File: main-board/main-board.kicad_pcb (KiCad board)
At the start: 2 copper layers, 210 x 130 mm, 173 parts, among them J1 PWR_SELECT, J10 Conn_02x05_Odd_Even, J11 Conn_02x05_Odd_Even, J12 Conn_02x05_Odd_Even, J13 Conn_02x05_Odd_Even, J14 Conn_02x05_Odd_Even, J15 Conn_02x05_Odd_Even, J16 COMM_3, J17 Modular board connector, J18 PWR_EXT_1, J19 PWR_EXT_2, J2 COMM1, J20 COMM_4, J21 COMM_OUT, J3 ICSP, J4 PULLUP_SEL, J5 COMM_2, J6 PULLDN_SEL, J7 Conn_02x05_Odd_Even, J8 Conn_02x05_Odd_Even, J9 Conn_02x05_Odd_Even, SW1 RESET, SW10 SW_Push, SW11 SW_Push, SW12 SW_SP3T_x08, SW13 SW_Push, SW14 SW_Push, SW15 SW_Push, SW16 SW_Push, SW17 SW_Push, SW18 SW_Push, SW19 SW_Push, SW2 BTN_LEVEL, SW20 SW_Push, SW21 SW_SP3T_x08, SW22 SW_Push, SW23 SW_Push, SW24 SW_Push, SW25 SW_Push, SW26 SW_Push, SW27 SW_Push, SW28 SW_Push, SW29 SW_Push, SW3 LED_GND, SW30 SW_SP3T_x08, SW31 SW_Push, SW32 SW_Push, SW33 SW_Push, SW34 SW_Push, SW35 SW_Push, SW36 SW_Push, SW37 SW_Push, SW38 SW_Push, SW39 SW_SP3T_x08, SW4 SW_Push, SW41 PWR_EN, SW5 SW_Push, SW6 SW_Push, SW7 SW_Push, SW8 SW_Push, SW9 SW_Push, U1 LM2576HVS-5, U2 AP1117-33, U3 AP1117-18, U4 FT232RL

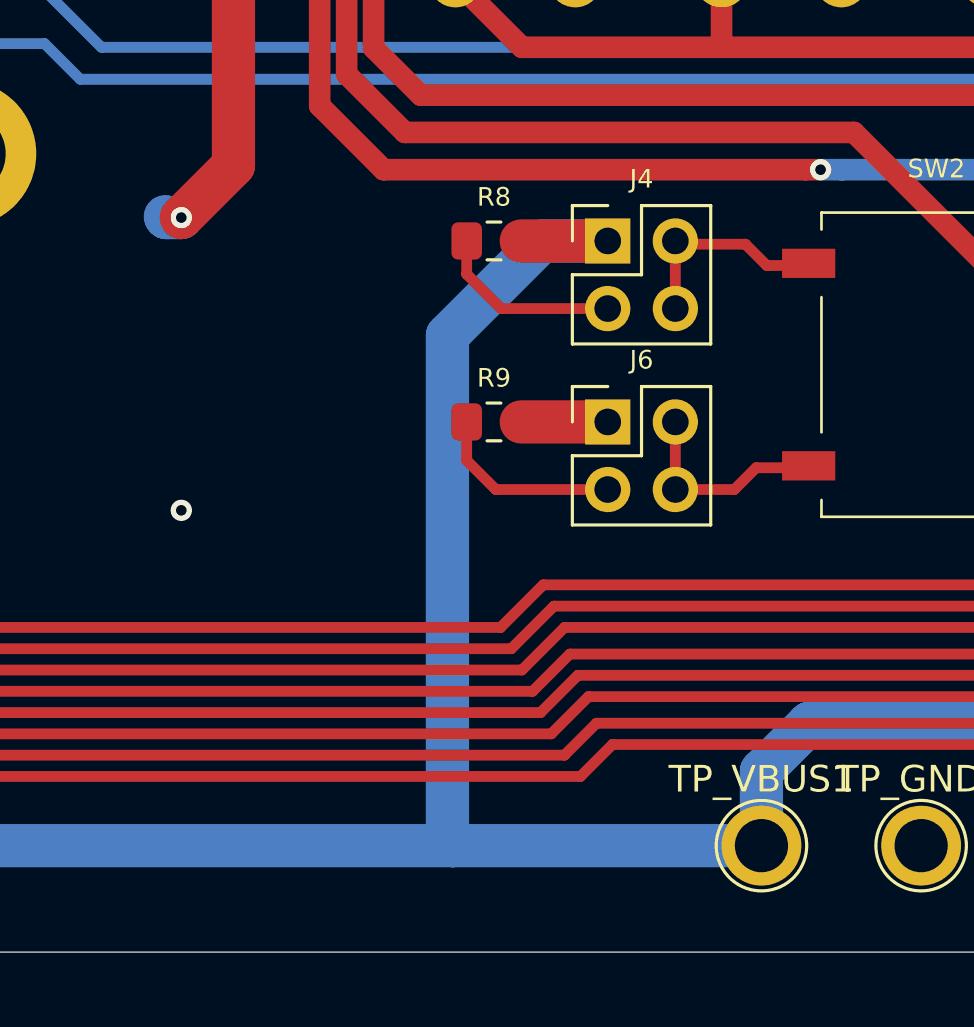
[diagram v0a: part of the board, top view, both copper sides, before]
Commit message: Changed button pullup-down selector
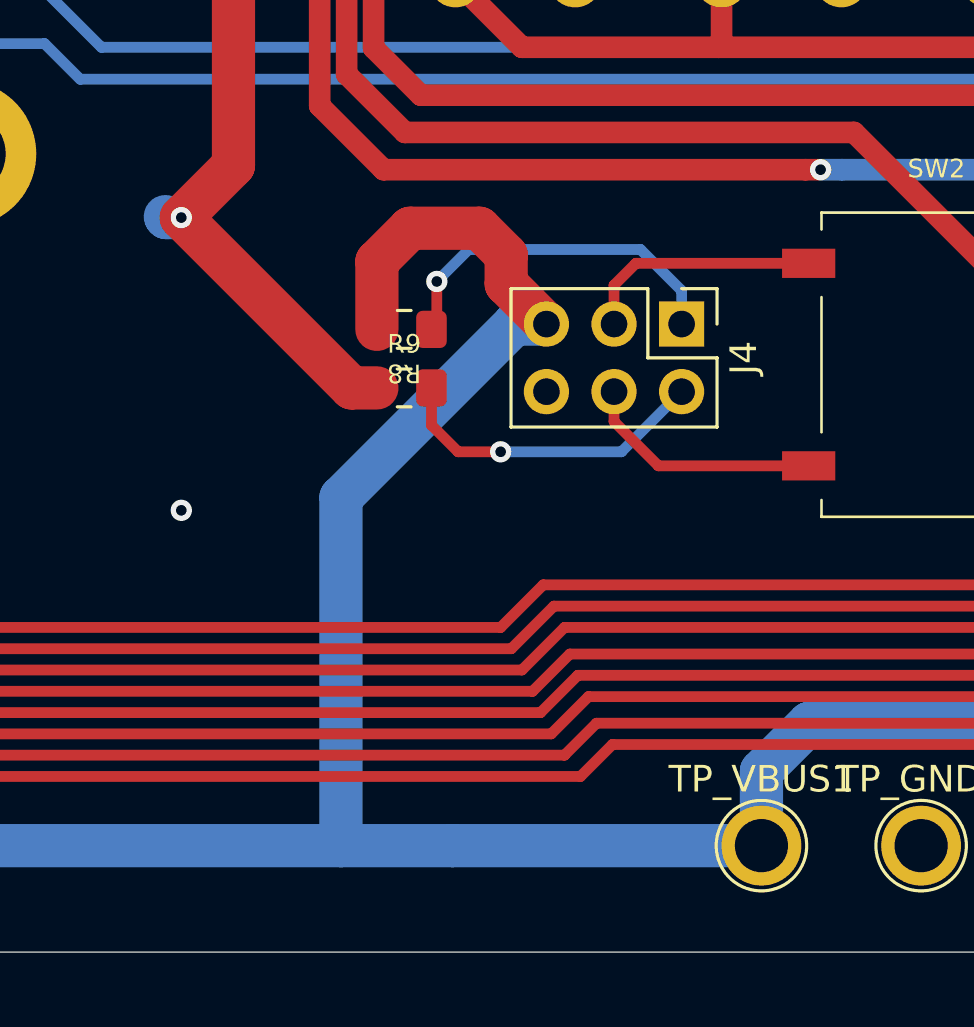
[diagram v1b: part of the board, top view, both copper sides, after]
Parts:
- removed J6: PULLDN_SEL, Connector_PinHeader_2.54mm:PinHeader_2x02_P2.54mm_Vertical
- J4: value PULLUP_SEL -> Conn_02x03_Top_Bottom; footprint Connector_PinHeader_2.54mm:PinHeader_2x02_P2.54mm_Vertical -> Connector_PinHeader_2.54mm:PinHeader_2x03_P2.54mm_Vertical
- moved R8 4.73 mm to (143.6, 124.6), turned to 180 degrees
- moved J4 4.18 mm to (154.0, 124.4), turned to 270 degrees
- moved R9 3.61 mm to (143.6, 126.8)
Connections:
- J4 pad 1: VBUS -> Net-(J4-Pad1)
- J4 pad 4: Net-(J4-Pad2) -> Net-(J4-Pad4)
- R8 pad 1: Net-(J4-Pad3) -> Net-(J4-Pad1)
- R9 pad 1: Net-(J6-Pad3) -> GND
- R9 pad 2: GND -> Net-(J4-Pad2)
- SW2 pad +: Net-(J4-Pad2) -> Net-(J4-Pad3)
- SW2 pad -: Net-(J6-Pad2) -> Net-(J4-Pad4)
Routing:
- net Net-(J4-Pad1): track 0.00 -> 13.5 mm, vias 0 -> 1
- net Net-(J4-Pad4): track 0.00 -> 9.23 mm
- net Net-(J6-Pad2): track 7.92 -> 0.00 mm
- net Net-(J6-Pad3): track 7.20 -> 0.00 mm
- net GND: track 113.6 -> 120.3 mm
- net Net-(J4-Pad2): track 7.97 -> 12.2 mm, vias 0 -> 1
- net VBUS: track 883.1 -> 886.8 mm
- net Net-(J4-Pad3): track 7.08 -> 9.23 mm

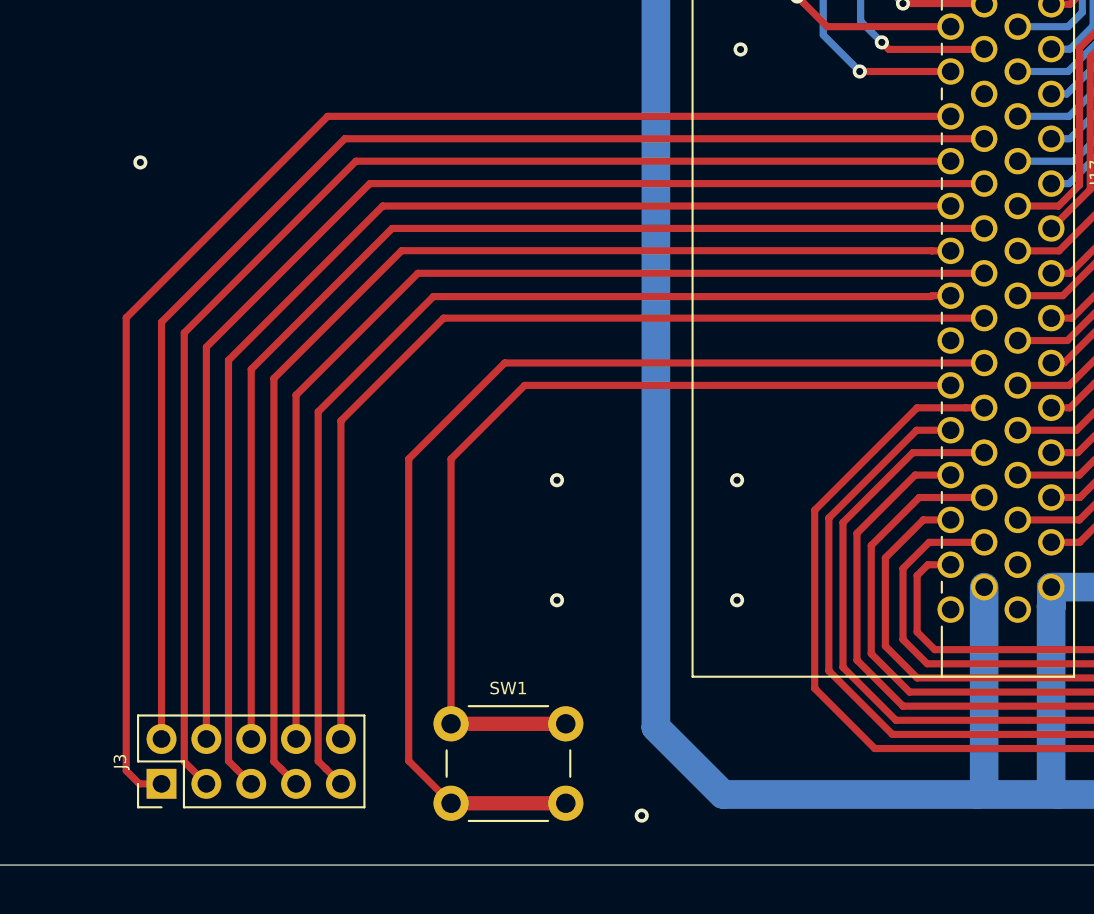
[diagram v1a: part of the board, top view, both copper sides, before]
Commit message: Rotated isp connector
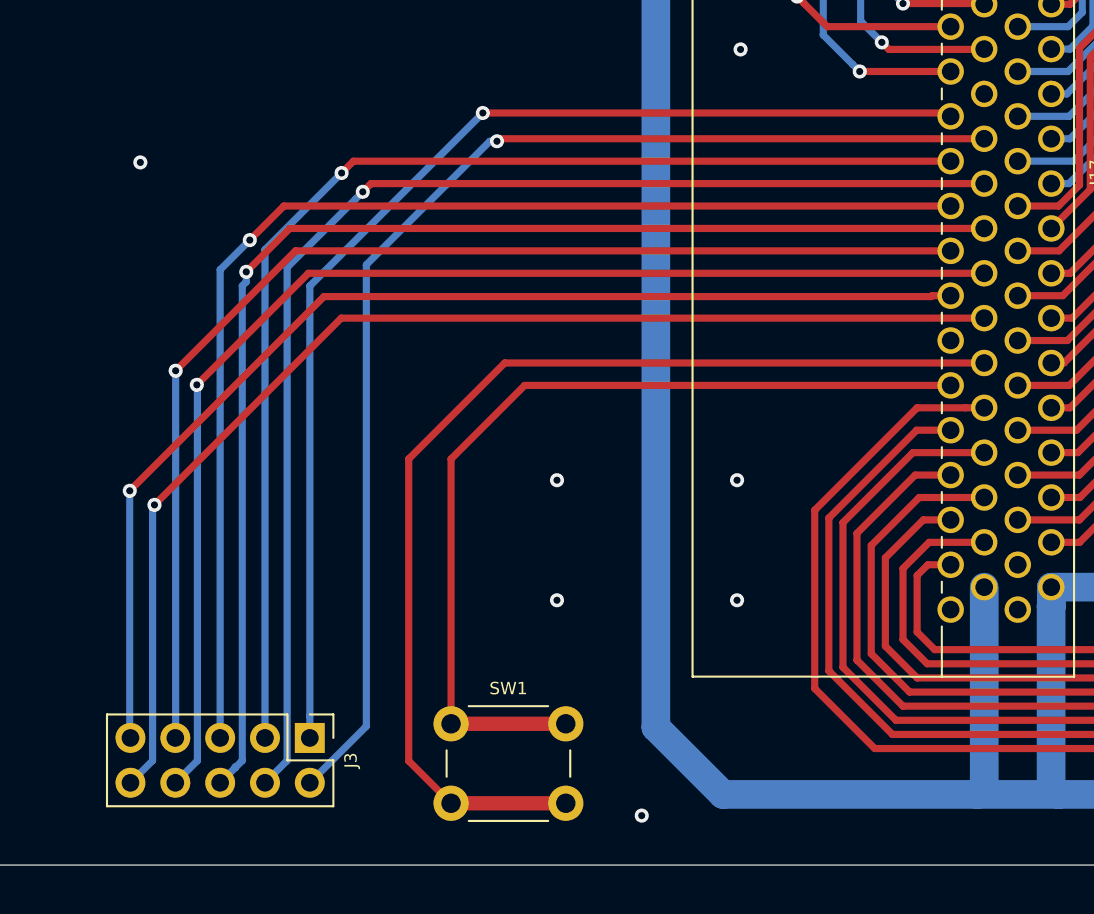
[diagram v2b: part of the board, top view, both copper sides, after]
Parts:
- moved J3 8.79 mm to (66.0, 140.8), turned to 270 degrees
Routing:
- net ICSP1: track 79.4 -> 66.0 mm, vias 0 -> 1
- net ICSP10: track 56.9 -> 67.7 mm, vias 0 -> 1
- net ICSP8: track 61.3 -> 70.3 mm, vias 0 -> 1
- net ICSP6: track 65.8 -> 72.4 mm, vias 0 -> 1
- net ICSP2: track 74.5 -> 68.6 mm, vias 0 -> 1
- net ICSP9: track 60.2 -> 65.1 mm, vias 0 -> 1
- net ICSP3: track 73.5 -> 68.6 mm, vias 0 -> 1
- net ICSP7: track 64.8 -> 67.5 mm, vias 0 -> 1
- net ICSP4: track 70.1 -> 71.2 mm, vias 0 -> 1
- net ICSP5: track 69.1 -> 69.4 mm, vias 0 -> 1

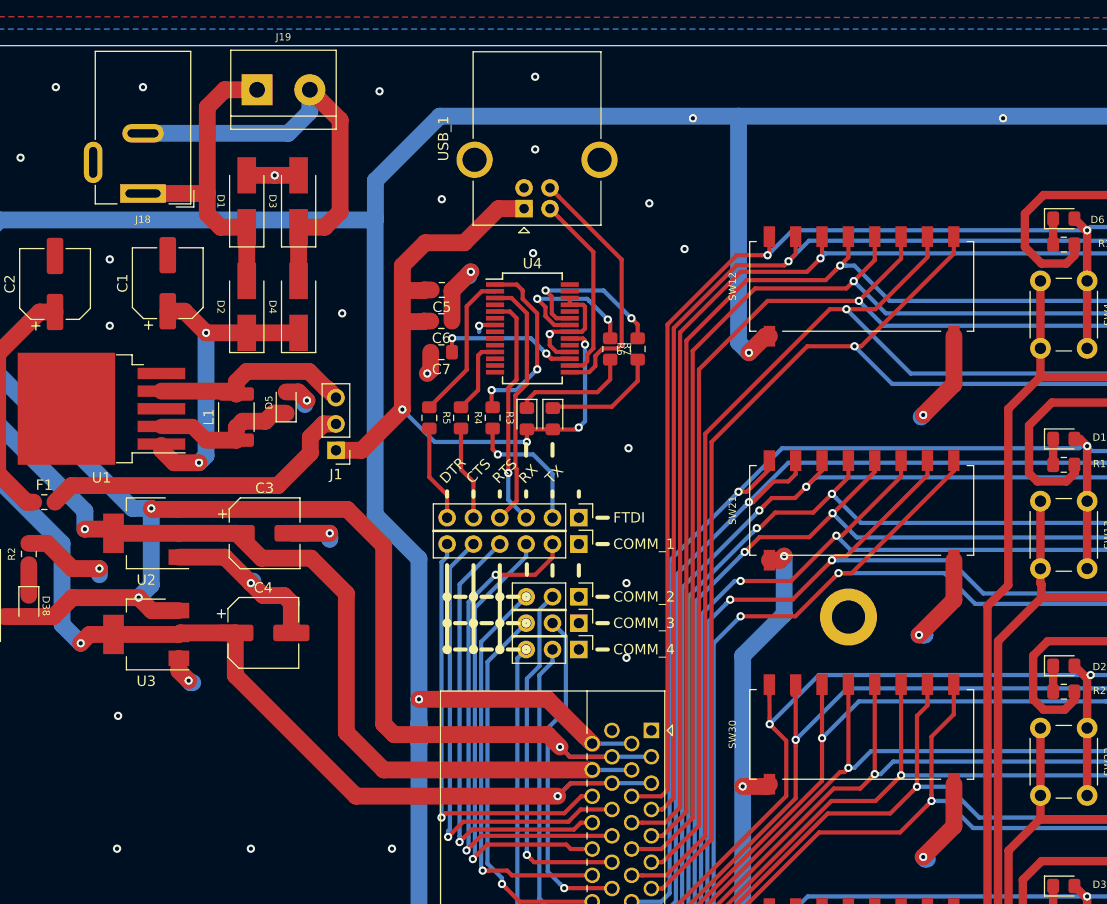
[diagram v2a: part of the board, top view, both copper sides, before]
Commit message: Added filled zones
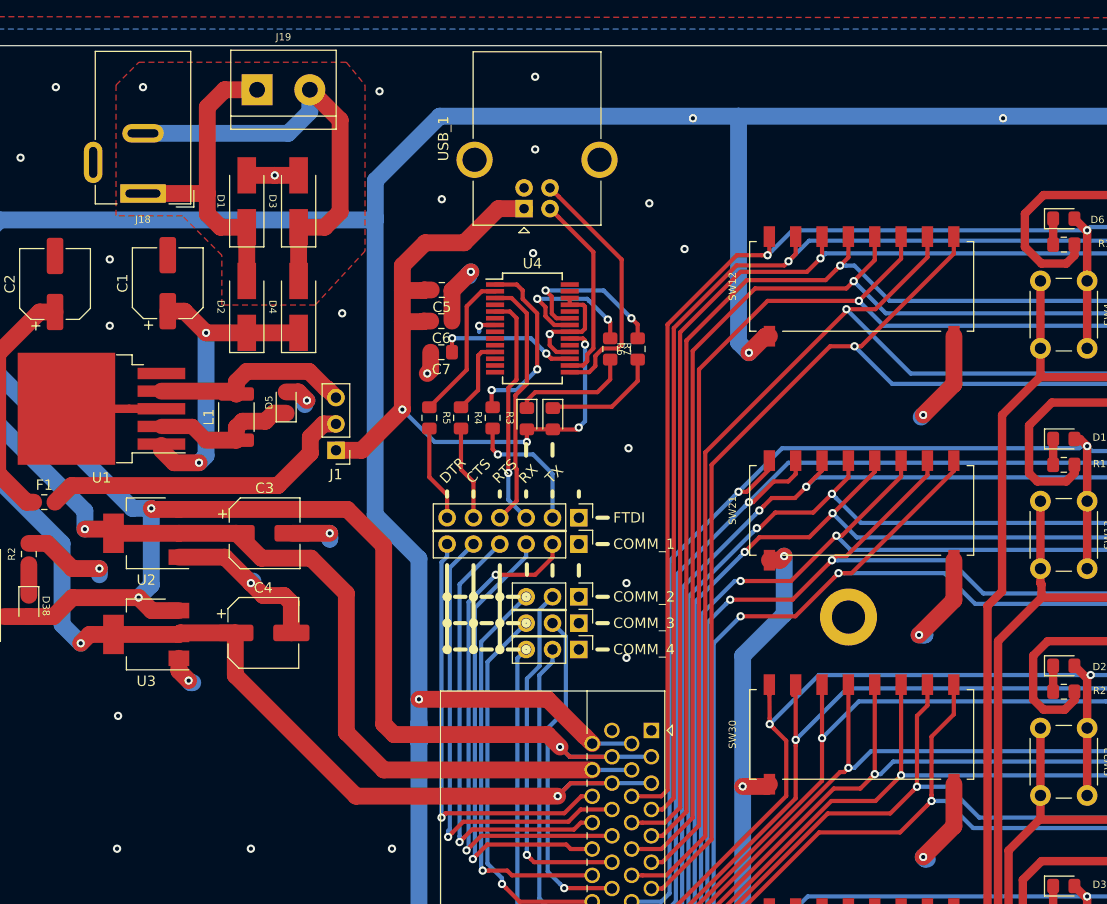
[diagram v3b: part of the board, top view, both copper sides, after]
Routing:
- net GND: track 120.3 -> 129.5 mm
- net /PORT_A_PIN8: track 214.9 -> 213.6 mm
- net /PORT_A_PIN7: track 214.3 -> 213.3 mm
- added copper zone on F.Cu, net Net-(D1-Pad1)
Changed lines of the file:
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@@
     (thickness 1.6)
     (drawings 78)
-    (tracks 2025)
+    (tracks 2027)
     (zones 0)
     (modules 172)
@@
   )
   (setup
-    (last_trace_width 0.4064)
+    (last_trace_width 0.8128)
     (user_trace_width 0.2032)
     (user_trace_width 0.4064)
@@
   (segment (start 141.6 126.8) (end 135.2 120.4) (width 1.6256) (layer F.Cu) (net 1))
   (segment (start 142.55 126.8) (end 141.6 126.8) (width 1.6256) (layer F.Cu) (net 1))
+  (segment (start 57.6622 53) (end 51.625 53) (width 0.8128) (layer F.Cu) (net 1))
+  (segment (start 60.775 53) (end 57.6622 53) (width 0.8128) (layer F.Cu) (net 1))
   (segment (start 59.8344 72.45) (end 62.46 72.45) (width 1.6256) (layer F.Cu) (net 2) (status 20))
   (segment (start 100.14 86.54) (end 99.2 85.6) (width 0.4064) (layer F.Cu) (net 2) (status 40000))
@@
   (segment (start 210 49.6) (end 210 47.175) (width 0.4064) (layer B.Cu) (net 88))
   (segment (start 212.425 49.6) (end 210 49.6) (width 0.4064) (layer B.Cu) (net 88))
-  (segment (start 107.16066 97.97) (end 106.1 97.97) (width 0.4064) (layer F.Cu) (net 88))
-  (segment (start 109.43 97.97) (end 107.16066 97.97) (width 0.4064) (layer F.Cu) (net 88))
-  (segment (start 113.193589 94.206411) (end 109.43 97.97) (width 0.4064) (layer F.Cu) (net 88))
-  (segment (start 113.193589 55.406411) (end 113.193589 94.206411) (width 0.4064) (layer F.Cu) (net 88))
-  (segment (start 126.796799 43.403201) (end 125.196799 43.403201) (width 0.4064) (layer F.Cu) (net 88))
-  (segment (start 125.196799 43.403201) (end 113.193589 55.406411) (width 0.4064) (layer F.Cu) (net 88))
   (segment (start 129.596799 43.403201) (end 126.796799 43.403201) (width 0.4064) (layer F.Cu) (net 88))
   (segment (start 134.61 36.405) (end 134.61 38.39) (width 0.4064) (layer F.Cu) (net 88))
   (segment (start 134.61 38.39) (end 129.596799 43.403201) (width 0.4064) (layer F.Cu) (net 88))
+  (segment (start 107.16066 97.97) (end 106.1 97.97) (width 0.4064) (layer F.Cu) (net 88))
+  (segment (start 109.43 97.97) (end 107.16066 97.97) (width 0.4064) (layer F.Cu) (net 88))
+  (segment (start 113.193589 94.206411) (end 109.43 97.97) (width 0.4064) (layer F.Cu) (net 88))
+  (segment (start 113.193589 57.206411) (end 113.193589 94.206411) (width 0.4064) (layer F.Cu) (net 88))
+  (segment (start 126.796799 43.403201) (end 126.796799 43.603201) (width 0.4064) (layer F.Cu) (net 88))
+  (segment (start 126.796799 43.603201) (end 113.193589 57.206411) (width 0.4064) (layer F.Cu) (net 88))
   (segment (start 240.450001 43.949999) (end 241.3 43.1) (width 0.4064) (layer B.Cu) (net 89))
   (segment (start 240.046799 44.353201) (end 240.450001 43.949999) (width 0.4064) (layer B.Cu) (net 89))
@@
   (segment (start 131.2 50.6) (end 127.5775 46.9775) (width 0.4064) (layer B.Cu) (net 89))
   (segment (start 221.2 50.6) (end 131.2 50.6) (width 0.4064) (layer B.Cu) (net 89))
-  (segment (start 109.06066 99.24) (end 108 99.24) (width 0.4064) (layer F.Cu) (net 89))
-  (segment (start 113.8 94.50066) (end 109.06066 99.24) (width 0.4064) (layer F.Cu) (net 89))
-  (segment (start 113.8 56.2) (end 113.8 94.50066) (width 0.4064) (layer F.Cu) (net 89))
-  (segment (start 127.5775 46.9775) (end 123.0225 46.9775) (width 0.4064) (layer F.Cu) (net 89))
-  (segment (start 123.0225 46.9775) (end 113.8 56.2) (width 0.4064) (layer F.Cu) (net 89))
   (via (at 221.2 50.6) (size 0.8) (drill 0.4) (layers F.Cu B.Cu) (net 89))
   (segment (start 220 47.175) (end 220 49.4) (width 0.4064) (layer F.Cu) (net 89))
@@
   (segment (start 137.15 36.405) (end 137.15 38.05) (width 0.4064) (layer F.Cu) (net 89))
   (segment (start 137.15 38.05) (end 128.2225 46.9775) (width 0.4064) (layer F.Cu) (net 89))
+  (segment (start 109.06066 99.24) (end 108 99.24) (width 0.4064) (layer F.Cu) (net 89))
+  (segment (start 113.8 94.50066) (end 109.06066 99.24) (width 0.4064) (layer F.Cu) (net 89))
+  (segment (start 113.8 58.4) (end 113.8 94.50066) (width 0.4064) (layer F.Cu) (net 89))
+  (segment (start 127.5775 46.9775) (end 125.2225 46.9775) (width 0.4064) (layer F.Cu) (net 89))
+  (segment (start 125.2225 46.9775) (end 113.8 58.4) (width 0.4064) (layer F.Cu) (net 89))
   (via (at 116.4 61) (size 0.8) (drill 0.4) (layers F.Cu B.Cu) (net 90))
   (segment (start 116.000001 61.399999) (end 116.4 61) (width 0.4064) (layer B.Cu) (net 90))
@@
   (segment (start 155.4625 49.9375) (end 145.4625 49.9375) (width 0.8128) (layer F.Cu) (net 112))
   (segment (start 158.655914 118.6) (end 159.221599 118.6) (width 0.8128) (layer F.Cu) (net 112))
-  (segment (start 142.4 53) (end 142.4 70) (width 0.8128) (layer F.Cu) (net 112))
-  (segment (start 145.4625 49.9375) (end 142.4 53) (width 0.8128) (layer F.Cu) (net 112))
-  (segment (start 142.4 70) (end 140.4 72) (width 0.8128) (layer F.Cu) (net 112))
-  (segment (start 140.4 116.2) (end 142.8 118.6) (width 0.8128) (layer F.Cu) (net 112))
+  (segment (start 141.8 53.6) (end 141.8 70.6) (width 0.8128) (layer F.Cu) (net 112))
+  (segment (start 145.4625 49.9375) (end 141.8 53.6) (width 0.8128) (layer F.Cu) (net 112))
   (segment (start 140.4 72) (end 140.4 116.2) (width 0.8128) (layer F.Cu) (net 112))
+  (segment (start 140.4 116.2) (end 142.8 118.6) (width 0.8128) (layer F.Cu) (net 112))
+  (segment (start 141.8 70.6) (end 140.4 72) (width 0.8128) (layer F.Cu) (net 112))
   (segment (start 142.8 118.6) (end 158.655914 118.6) (width 0.8128) (layer F.Cu) (net 112))
   (segment (start 48 70.975) (end 48 68.025) (width 1.6256) (layer F.Cu) (net 113) (status 30))
@@
       )
     )
+  )
+  (zone (net 10) (net_name "Net-(D1-Pad1)") (layer F.Cu) (hatch edge 0.508)
+    (priority 2)
+    (connect_pads (clearance 0.808))
+    (min_thickness 0.254)
+    (fill yes (arc_segments 32) (thermal_gap 0.508) (thermal_bridge_width 0.508))
+    (polygon
+      (pts
+        (xy 80.4 21.8) (xy 80.4 37.8) (xy 75.6 43) (xy 66.6 43) (xy 66.6 38.2)
+        (xy 62.8 34.4) (xy 56.4 34.4) (xy 56.4 21.8) (xy 58.6 19.6) (xy 78.6 19.6)
+      )
+    )
